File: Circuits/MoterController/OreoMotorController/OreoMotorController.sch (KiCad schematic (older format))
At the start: 19 parts

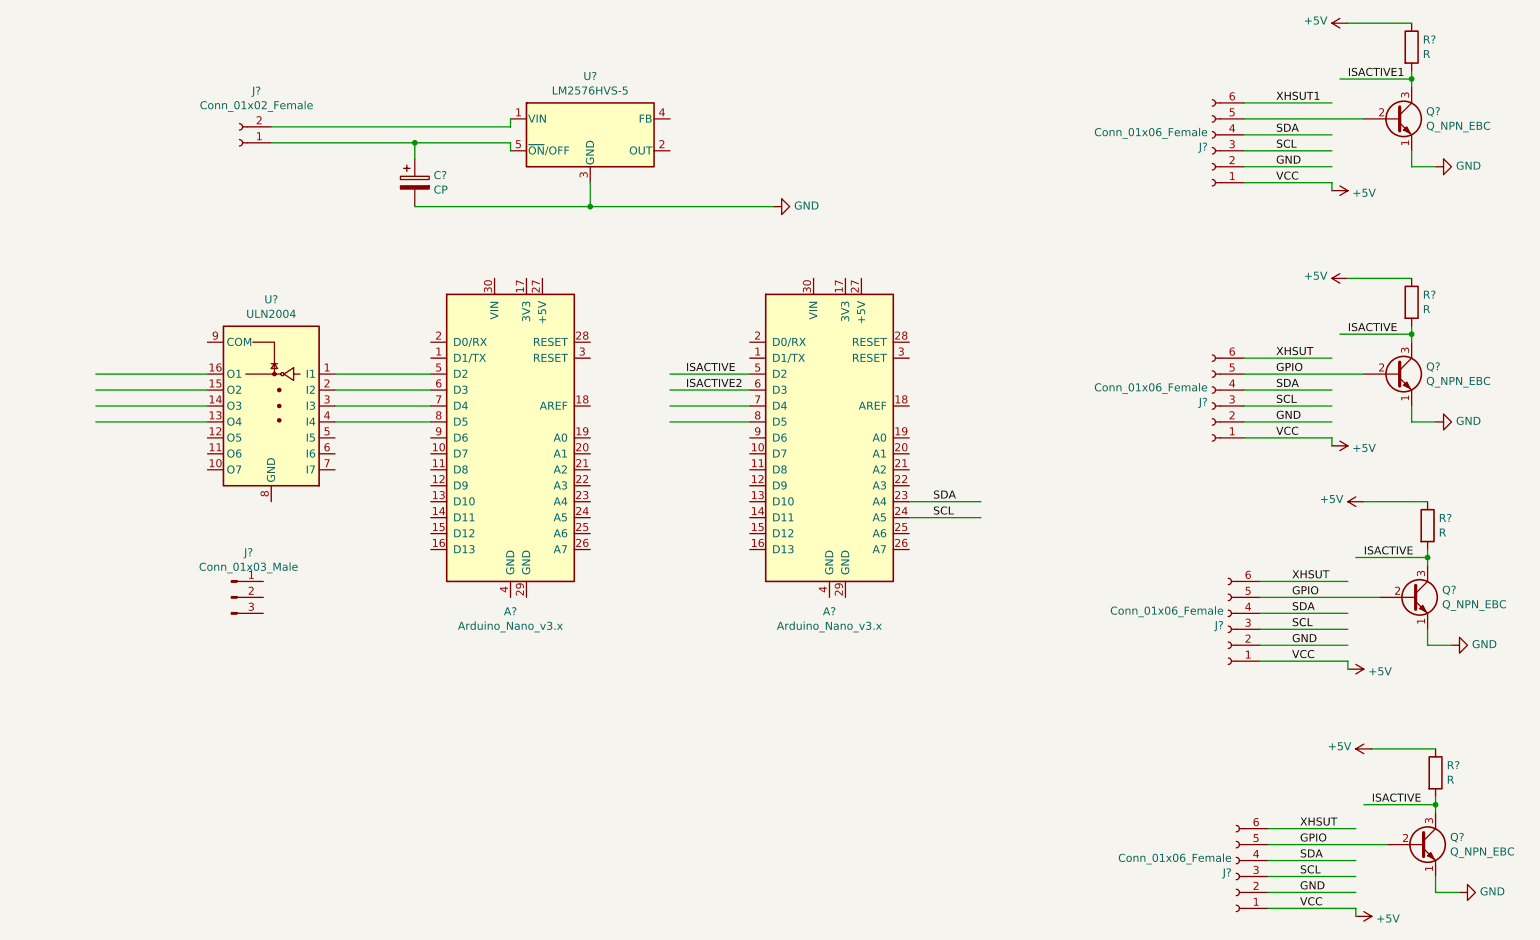
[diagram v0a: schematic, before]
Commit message: add : circuit, CNN, Arduino
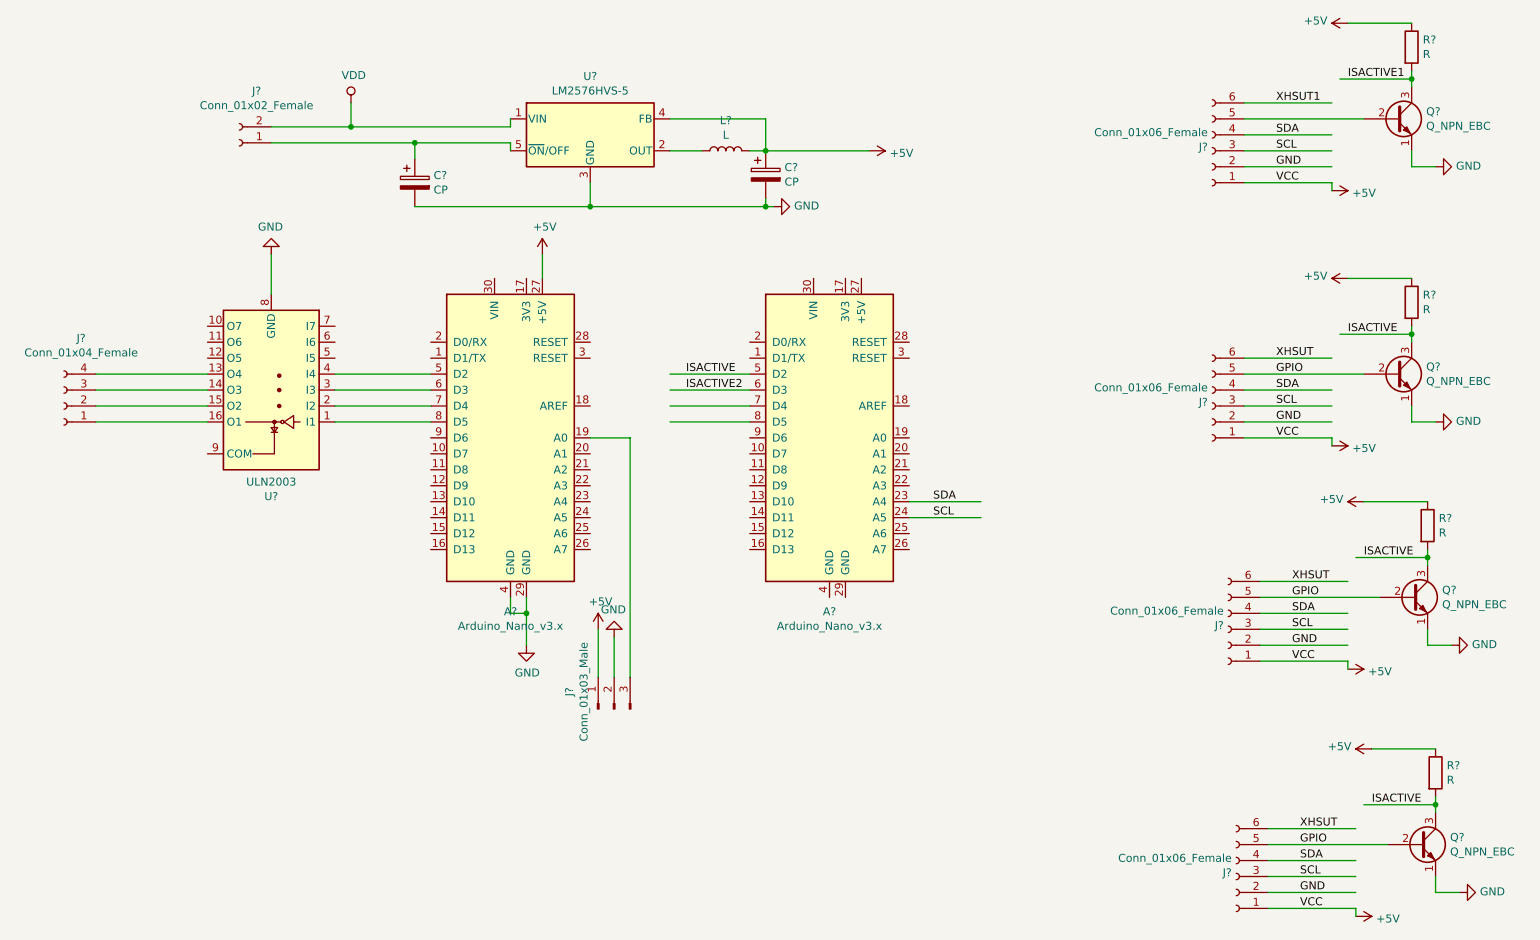
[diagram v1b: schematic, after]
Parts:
- removed U?: ULN2004, symbol Transistor_Array:ULN2004
- added C?: CP, symbol Device:CP
- added J?: Conn_01x04_Female, symbol Connector:Conn_01x04_Female
- added L?: L, symbol Device:L
- added U?: ULN2003, symbol Transistor_Array:ULN2003
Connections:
- net labels added: VDD
- wire segments 75 -> 94
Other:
- moved on the sheet: J?
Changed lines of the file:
@@
 EESchema Schematic File Version 4
+LIBS:OreoMotorController-cache
 EELAYER 29 0
 EELAYER END
@@
 	1    0    0    -1
 $EndComp
-$Comp
-L Transistor_Array:ULN2004 U?
-U 1 1 5D126CB4
-P 3300 3150
-F 0 "U?" H 3300 3817 50  0000 C CNN
-F 1 "ULN2004" H 3300 3726 50  0000 C CNN
-F 2 "" H 3350 2600 50  0001 L CNN
-F 3 "http://www.ti.com/lit/ds/symlink/uln2003a.pdf" H 3400 2950 50  0001 C CNN
-	1    3300 3150
-	-1   0    0    -1
-$EndComp
 Wire Wire Line
 	4300 2950 3700 2950
@@
 Connection ~ 5300 1900
 Wire Wire Line
-	5300 1900 6450 1900
-$Comp
-L power:GND #PWR?
+	5300 1900 6400 1900
+$Comp
+L power:GND #PWR0101
 U 1 1 5D137893
 P 6450 1900
-F 0 "#PWR?" H 6450 1650 50  0001 C CNN
+F 0 "#PWR0101" H 6450 1650 50  0001 C CNN
 F 1 "GND" V 6455 1772 50  0000 R CNN
 F 2 "" H 6450 1900 50  0001 C CNN
@@
 $EndComp
 Wire Wire Line
-	3300 1400 4800 1400
+	3300 1400 3800 1400
 Wire Wire Line
 	4800 1400 4800 1350
@@
 L Connector:Conn_01x03_Male J?
 U 1 1 5D1446B5
-P 3050 4350
-F 0 "J?" H 3158 4631 50  0000 C CNN
-F 1 "Conn_01x03_Male" H 3158 4540 50  0000 C CNN
-F 2 "" H 3050 4350 50  0001 C CNN
-F 3 "~" H 3050 4350 50  0001 C CNN
-	1    3050 4350
-	1    0    0    -1
+P 5450 5050
+F 0 "J?" H 5558 5331 50  0000 C CNN
+F 1 "Conn_01x03_Male" H 5558 5240 50  0000 C CNN
+F 2 "" H 5450 5050 50  0001 C CNN
+F 3 "~" H 5450 5050 50  0001 C CNN
+	1    5450 5050
+	0    -1   -1   0
 $EndComp
 $Comp
@@
 XHSUT
 $Comp
-L power:+5V #PWR?
+L power:+5V #PWR0102
 U 1 1 5D152B9E
 P 9950 3400
-F 0 "#PWR?" H 9950 3250 50  0001 C CNN
+F 0 "#PWR0102" H 9950 3250 50  0001 C CNN
 F 1 "+5V" V 9965 3528 50  0000 L CNN
 F 2 "" H 9950 3400 50  0001 C CNN
@@
 	10450 2650 10450 2700
 $Comp
-L power:GND #PWR?
+L power:GND #PWR0103
 U 1 1 5D16A29B
 P 10600 3250
-F 0 "#PWR?" H 10600 3000 50  0001 C CNN
+F 0 "#PWR0103" H 10600 3000 50  0001 C CNN
 F 1 "GND" V 10605 3122 50  0000 R CNN
 F 2 "" H 10600 3250 50  0001 C CNN
@@
 	10450 3250 10600 3250
 $Comp
-L power:+5V #PWR?
+L power:+5V #PWR0104
 U 1 1 5D16ACA0
 P 10050 2350
-F 0 "#PWR?" H 10050 2200 50  0001 C CNN
+F 0 "#PWR0104" H 10050 2200 50  0001 C CNN
 F 1 "+5V" V 10065 2478 50  0000 L CNN
 F 2 "" H 10050 2350 50  0001 C CNN
@@
 XHSUT1
 $Comp
-L power:+5V #PWR?
+L power:+5V #PWR0105
 U 1 1 5D178EC3
 P 9950 1800
-F 0 "#PWR?" H 9950 1650 50  0001 C CNN
+F 0 "#PWR0105" H 9950 1650 50  0001 C CNN
 F 1 "+5V" V 9965 1928 50  0000 L CNN
 F 2 "" H 9950 1800 50  0001 C CNN
@@
 	10450 1050 10450 1100
 $Comp
-L power:GND #PWR?
+L power:GND #PWR0106
 U 1 1 5D178EE3
 P 10600 1650
-F 0 "#PWR?" H 10600 1400 50  0001 C CNN
+F 0 "#PWR0106" H 10600 1400 50  0001 C CNN
 F 1 "GND" V 10605 1522 50  0000 R CNN
 F 2 "" H 10600 1650 50  0001 C CNN
@@
 	10450 1650 10600 1650
 $Comp
-L power:+5V #PWR?
+L power:+5V #PWR0107
 U 1 1 5D178EEF
 P 10050 750
-F 0 "#PWR?" H 10050 600 50  0001 C CNN
+F 0 "#PWR0107" H 10050 600 50  0001 C CNN
 F 1 "+5V" V 10065 878 50  0000 L CNN
 F 2 "" H 10050 750 50  0001 C CNN
@@
 XHSUT
 $Comp
-L power:+5V #PWR?
+L power:+5V #PWR0108
 U 1 1 5D17F289
 P 10050 4800
-F 0 "#PWR?" H 10050 4650 50  0001 C CNN
+F 0 "#PWR0108" H 10050 4650 50  0001 C CNN
 F 1 "+5V" V 10065 4928 50  0000 L CNN
 F 2 "" H 10050 4800 50  0001 C CNN
@@
 	10550 4050 10550 4100
 $Comp
-L power:GND #PWR?
+L power:GND #PWR0109
 U 1 1 5D17F2A9
 P 10700 4650
-F 0 "#PWR?" H 10700 4400 50  0001 C CNN
+F 0 "#PWR0109" H 10700 4400 50  0001 C CNN
 F 1 "GND" V 10705 4522 50  0000 R CNN
 F 2 "" H 10700 4650 50  0001 C CNN
@@
 	10550 4650 10700 4650
 $Comp
-L power:+5V #PWR?
+L power:+5V #PWR0110
 U 1 1 5D17F2B5
 P 10150 3750
-F 0 "#PWR?" H 10150 3600 50  0001 C CNN
+F 0 "#PWR0110" H 10150 3600 50  0001 C CNN
 F 1 "+5V" V 10165 3878 50  0000 L CNN
 F 2 "" H 10150 3750 50  0001 C CNN
@@
 XHSUT
 $Comp
-L power:+5V #PWR?
+L power:+5V #PWR0111
 U 1 1 5D1871D3
 P 10100 6350
-F 0 "#PWR?" H 10100 6200 50  0001 C CNN
+F 0 "#PWR0111" H 10100 6200 50  0001 C CNN
 F 1 "+5V" V 10115 6478 50  0000 L CNN
 F 2 "" H 10100 6350 50  0001 C CNN
@@
 	10600 5600 10600 5650
 $Comp
-L power:GND #PWR?
+L power:GND #PWR0112
 U 1 1 5D1871F3
 P 10750 6200
-F 0 "#PWR?" H 10750 5950 50  0001 C CNN
+F 0 "#PWR0112" H 10750 5950 50  0001 C CNN
 F 1 "GND" V 10755 6072 50  0000 R CNN
 F 2 "" H 10750 6200 50  0001 C CNN
@@
 	10600 6200 10750 6200
 $Comp
-L power:+5V #PWR?
+L power:+5V #PWR0113
 U 1 1 5D1871FF
 P 10200 5300
-F 0 "#PWR?" H 10200 5150 50  0001 C CNN
+F 0 "#PWR0113" H 10200 5150 50  0001 C CNN
 F 1 "+5V" V 10215 5428 50  0000 L CNN
 F 2 "" H 10200 5300 50  0001 C CNN
@@
 Text Label 10200 5650 0    50   ~ 0
 ISACTIVE
+$Comp
+L Transistor_Array:ULN2003 U?
+U 1 1 5D276BEB
+P 3300 3050
+F 0 "U?" H 3300 3717 50  0000 C CNN
+F 1 "ULN2003" H 3300 3626 50  0000 C CNN
+F 2 "" H 3350 2500 50  0001 L CNN
+F 3 "http://www.ti.com/lit/ds/symlink/uln2003a.pdf" H 3400 2850 50  0001 C CNN
+	1    3300 3050
+	-1   0    0    1
+$EndComp
+$Comp
+L power:GND #PWR0114
+U 1 1 5D2895CE
+P 3300 2200
+F 0 "#PWR0114" H 3300 1950 50  0001 C CNN
+F 1 "GND" H 3305 2027 50  0000 C CNN
+F 2 "" H 3300 2200 50  0001 C CNN
+F 3 "" H 3300 2200 50  0001 C CNN
+	1    3300 2200
+	-1   0    0    1
+$EndComp
+Wire Wire Line
+	3300 2200 3300 2450
+$Comp
+L Device:L L?
+U 1 1 5D28C232
+P 6150 1550
+F 0 "L?" V 6340 1550 50  0000 C CNN
+F 1 "L" V 6249 1550 50  0000 C CNN
+F 2 "" H 6150 1550 50  0001 C CNN
+F 3 "~" H 6150 1550 50  0001 C CNN
+	1    6150 1550
+	0    -1   -1   0
+$EndComp
+$Comp
+L Device:CP C?
+U 1 1 5D28CB35
+P 6400 1700
+F 0 "C?" H 6518 1746 50  0000 L CNN
+F 1 "CP" H 6518 1655 50  0000 L CNN
+F 2 "" H 6438 1550 50  0001 C CNN
+F 3 "~" H 6400 1700 50  0001 C CNN
+	1    6400 1700
+	1    0    0    -1
+$EndComp
+Wire Wire Line
+	5800 1550 6000 1550
+Wire Wire Line
+	6300 1550 6400 1550
+Wire Wire Line
+	6400 1850 6400 1900
+Connection ~ 6400 1900
+Wire Wire Line
+	6400 1900 6450 1900
+Wire Wire Line
+	5800 1350 6400 1350
+Wire Wire Line
+	6400 1350 6400 1550
+Connection ~ 6400 1550
+Wire Wire Line
+	6400 1550 7050 1550
+$Comp
+L power:+5V #PWR0115
+U 1 1 5D297BD8
+P 7050 1550
+F 0 "#PWR0115" H 7050 1400 50  0001 C CNN
+F 1 "+5V" V 7065 1678 50  0000 L CNN
+F 2 "" H 7050 1550 50  0001 C CNN
+F 3 "" H 7050 1550 50  0001 C CNN
+	1    7050 1550
+	0    1    1    0
+$EndComp
+Wire Wire Line
+	5300 3350 5550 3350
+Wire Wire Line
+	5550 3350 5550 4850
+$Comp
+L power:+5V #PWR0116
+U 1 1 5D2A2702
+P 5350 4550
+F 0 "#PWR0116" H 5350 4400 50  0001 C CNN
+F 1 "+5V" H 5365 4723 50  0000 C CNN
+F 2 "" H 5350 4550 50  0001 C CNN
+F 3 "" H 5350 4550 50  0001 C CNN
+	1    5350 4550
+	1    0    0    -1
+$EndComp
+$Comp
+L power:GND #PWR0117
+U 1 1 5D2A2E3D
+P 5450 4600
+F 0 "#PWR0117" H 5450 4350 50  0001 C CNN
+F 1 "GND" H 5455 4427 50  0000 C CNN
+F 2 "" H 5450 4600 50  0001 C CNN
+F 3 "" H 5450 4600 50  0001 C CNN
+	1    5450 4600
+	-1   0    0    1
+$EndComp
+Wire Wire Line
+	5350 4550 5350 4850
+Wire Wire Line
+	5450 4600 5450 4850
+$Comp
+L power:+5V #PWR0118
+U 1 1 5D2AC0D9
+P 5000 2200
+F 0 "#PWR0118" H 5000 2050 50  0001 C CNN
+F 1 "+5V" H 5015 2373 50  0000 C CNN
+F 2 "" H 5000 2200 50  0001 C CNN
+F 3 "" H 5000 2200 50  0001 C CNN
+	1    5000 2200
+	1    0    0    -1
+$EndComp
+$Comp
+L power:GND #PWR0119
+U 1 1 5D2AC8D9
+P 4900 4650
+F 0 "#PWR0119" H 4900 4400 50  0001 C CNN
+F 1 "GND" H 4905 4477 50  0000 C CNN
+F 2 "" H 4900 4650 50  0001 C CNN
+F 3 "" H 4900 4650 50  0001 C CNN
+	1    4900 4650
+	1    0    0    -1
+$EndComp
+Wire Wire Line
+	4800 4350 4800 4450
+Wire Wire Line
+	4800 4450 4900 4450
+Wire Wire Line
+	4900 4450 4900 4650
+Wire Wire Line
+	4900 4350 4900 4450
+Connection ~ 4900 4450
+Wire Wire Line
+	5000 2350 5000 2200
+$Comp
+L Connector:Conn_01x04_Female J?
+U 1 1 5D2B7AFA
+P 2000 3150
+F 0 "J?" H 1892 2725 50  0000 C CNN
+F 1 "Conn_01x04_Female" H 1892 2816 50  0000 C CNN
+F 2 "" H 2000 3150 50  0001 C CNN
+F 3 "~" H 2000 3150 50  0001 C CNN
+	1    2000 3150
+	-1   0    0    1
+$EndComp
+$Comp
+L power:VDD #PWR0120
+U 1 1 5D2B8A4F
+P 3800 1250
+F 0 "#PWR0120" H 3800 1100 50  0001 C CNN
+F 1 "VDD" H 3817 1423 50  0000 C CNN
+F 2 "" H 3800 1250 50  0001 C CNN
+F 3 "" H 3800 1250 50  0001 C CNN
+	1    3800 1250
+	1    0    0    -1
+$EndComp
+Wire Wire Line
+	3800 1250 3800 1400
+Connection ~ 3800 1400
+Wire Wire Line
+	3800 1400 4800 1400
 $EndSCHEMATC
